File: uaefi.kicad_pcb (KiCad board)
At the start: 4 copper layers, 100 x 136 mm, 150 parts, among them J1 Conn_02x02_Odd_Even, J11 Conn_02x02_Odd_Even, J12 Conn_02x02_Odd_Even, J13 Conn_02x02_Odd_Even, J14 Conn_02x02_Odd_Even, J15 Conn_02x02_Odd_Even, J16 Conn_02x02_Odd_Even, J17 Conn_02x02_Odd_Even, J18 Conn_02x02_Odd_Even, J19 Conn_02x02_Odd_Even, J20 Conn_02x02_Odd_Even, J21 Conn_02x02_Odd_Even, J22 Conn_02x02_Odd_Even, J24 Conn_02x02_Odd_Even, J30 776163-1, J31 776163-1, J6 Conn_01x06, J7 Conn_01x05_Male, J8 USB_B_Mini, J9 USB_C, M1 Module-power_12and5V-0.3, M2 Module-knock-0.2, M3 Module-vr-discrete-0.5, M4 Module-vr-max9924-0.1, M5 Module-wbo-0.5, M6 Module:mega-mcu100/0.3, M7 Module-can-0.1, P1 Pad, P15 Pad, P16 Pad, P17 Pad, P18 Pad, P2 Pad, P3 Pad, P4 Pad, P5 Pad, P6 Pad, P7 Pad, P8 Pad, U1 TLE9201SG, U10 VNLD5160TR-E, U11 VNLD5160TR-E, U2 TLE9201SG, U3 MPX4/MPXH6400_MAP, U4 MAX31855KASA, U5 JDY-33, U6 VNLD5160TR-E, U7 VNLD5160TR-E, U8 VNLD5160TR-E, U9 VNLD5160TR-E

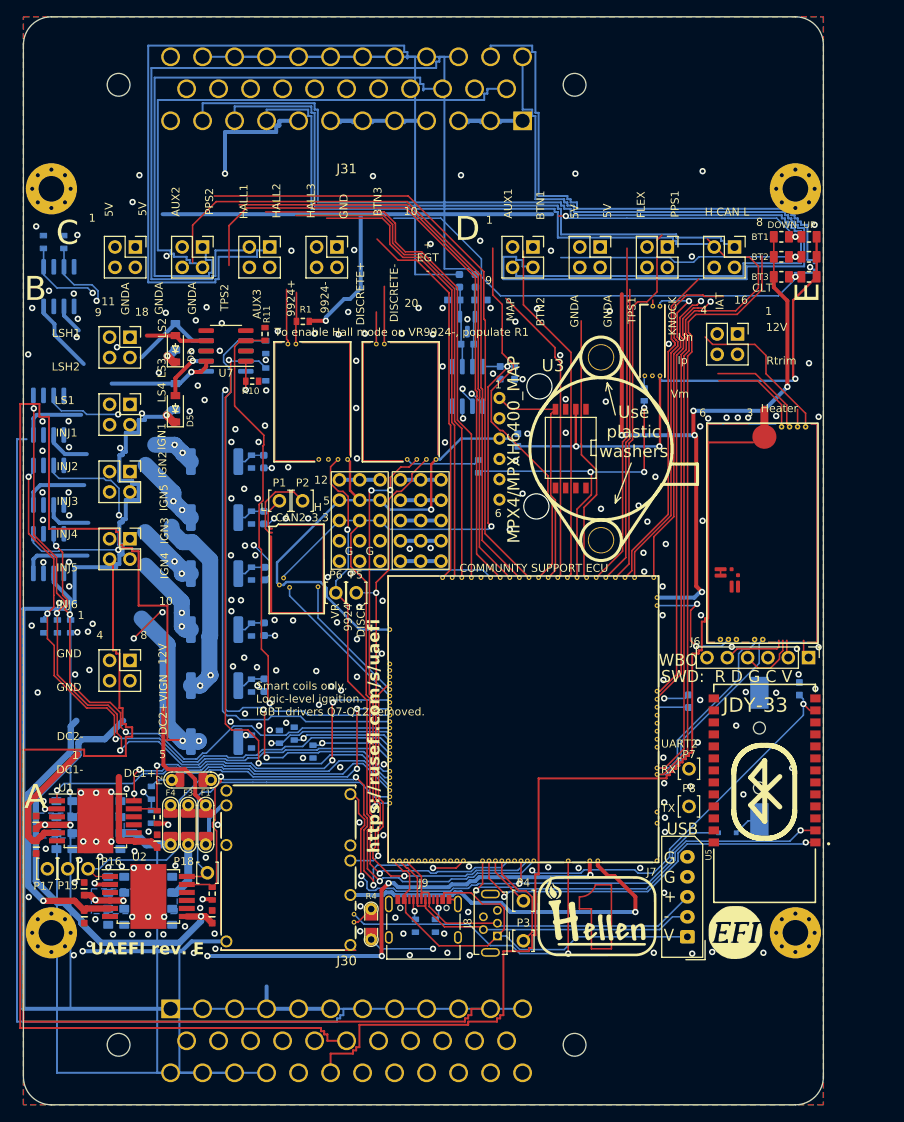
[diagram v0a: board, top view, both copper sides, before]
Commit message: Refill zones, route AMPSEAL pads without shorts, and export KiCad 8 fab files.
Co-authored-by: Quintin <quintinbannink42@users.noreply.github.com>
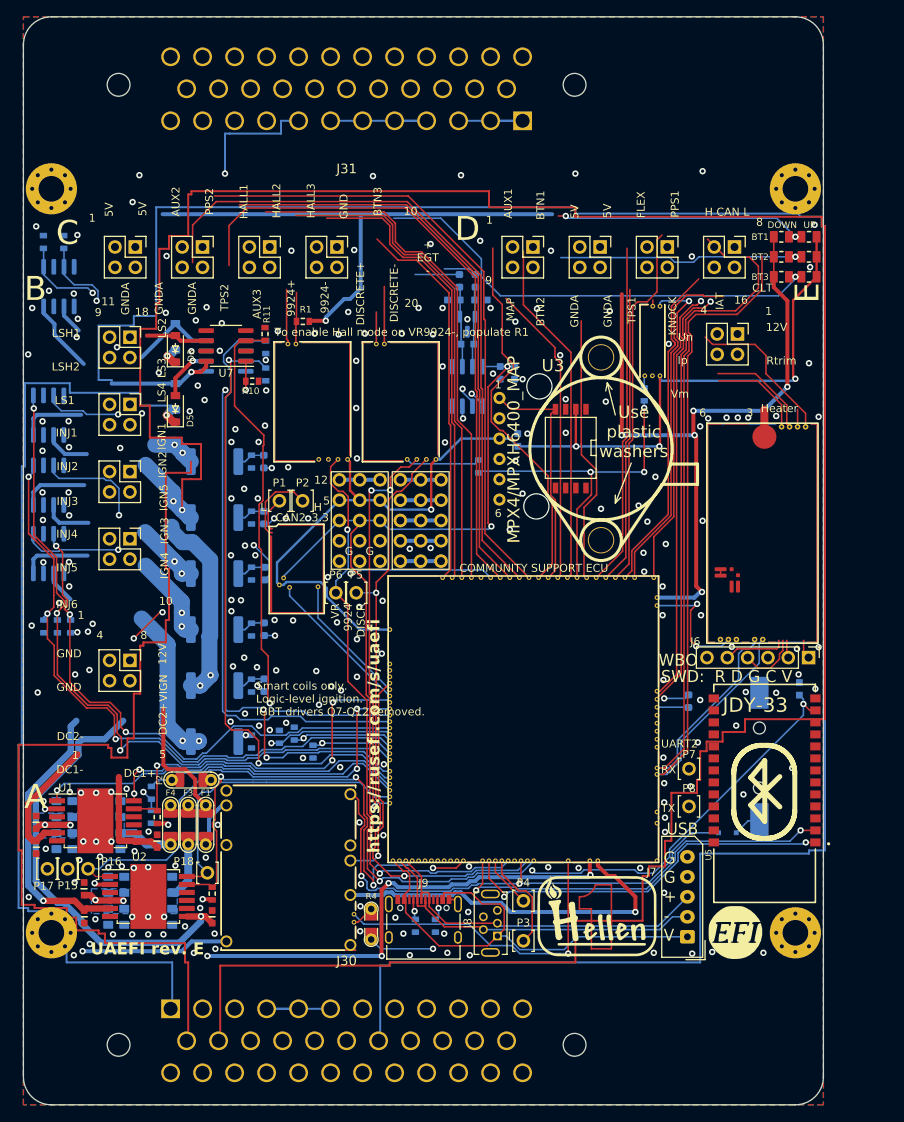
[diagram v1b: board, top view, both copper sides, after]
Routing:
- net /WBO_Rtrim: track 284.2 -> 2.19 mm
- net /OUT_LS4: track 211.3 -> 6.95 mm
- net /VR_DISCRETE+: track 201.0 -> 4.01 mm
- net /OUT_LS_HOT2: track 119.3 -> 314.8 mm
- net /OUT_IGN2: track 133.4 -> 326.4 mm
- net /OUT_LS2: track 190.5 -> 7.69 mm
- net /OUT_IGN6: track 201.9 -> 19.5 mm
- net /VR_MAX9924-: track 179.9 -> 6.49 mm
- net /VR_MAX9924+: track 167.5 -> 6.89 mm
- net /VR_DISCRETE-: track 150.2 -> 7.21 mm
- net /WBO_Ip: track 155.1 -> 13.1 mm
- net /OUT_INJ5: track 143.5 -> 282.9 mm
- net /WBO_Vm: track 150.3 -> 11.9 mm
- net /WBO_Un: track 156.3 -> 19.5 mm
- net /OUT_LS_HOT1: track 140.2 -> 3.77 mm
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
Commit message: Widen the board and route harness nets through a right-edge channel.
Co-authored-by: Quintin <quintinbannink42@users.noreply.github.com>
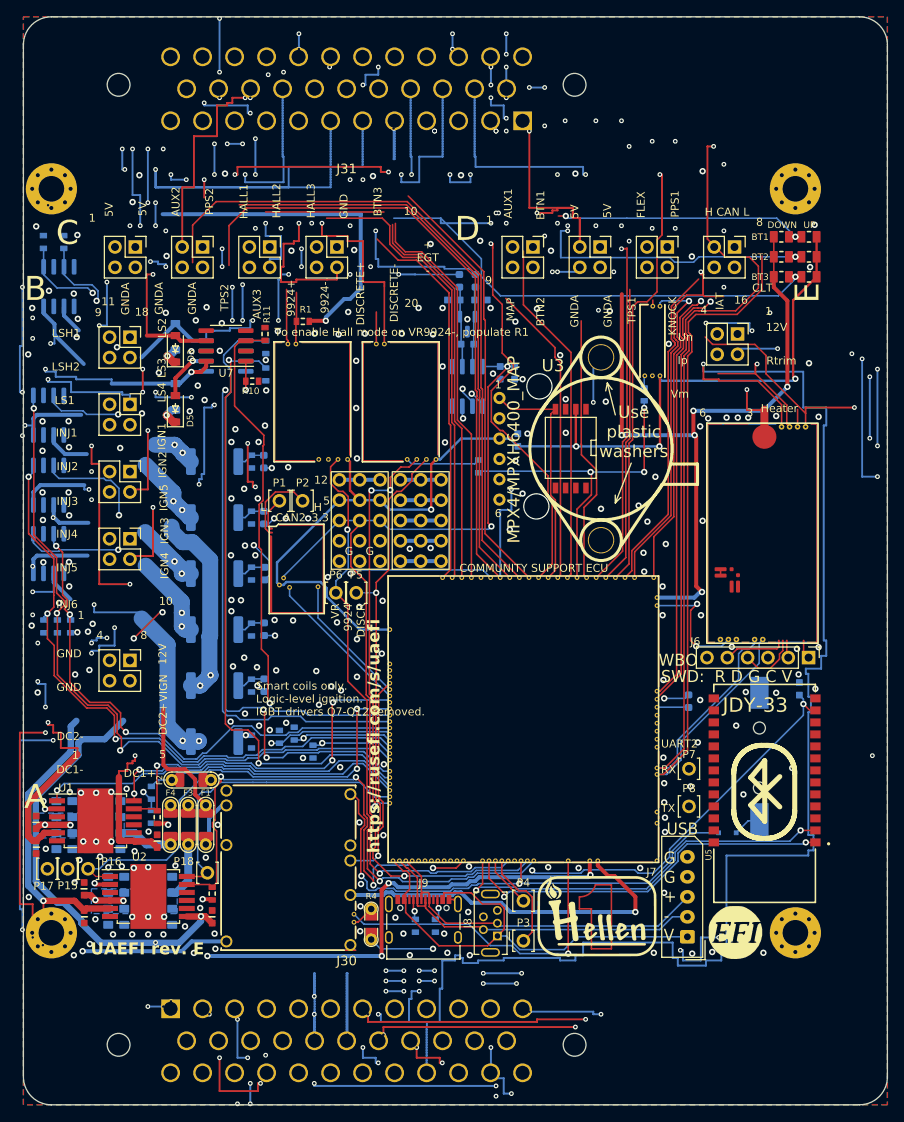
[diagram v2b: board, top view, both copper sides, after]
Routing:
- net /OUT_DC1-: track 17.1 -> 376.1 mm, vias 0 -> 5
- net /OUT_DC1+: track 13.1 -> 355.1 mm, vias 0 -> 5
- net /OUT_INJ6: track 4.09 -> 336.9 mm, vias 0 -> 9
- net /OUT_LS4: track 6.95 -> 338.3 mm, vias 1 -> 6
- net +12V: track 87.3 -> 403.6 mm, vias 0 -> 8
- net /OUT_IGN6: track 19.5 -> 317.7 mm, vias 2 -> 8
- net /OUT_LS2: track 7.69 -> 285.2 mm, vias 0 -> 7
- net /12V_KEY: track 105.2 -> 369.1 mm, vias 0 -> 8
- net /OUT_IGN5: track 24.4 -> 288.2 mm, vias 2 -> 6
- net /OUT_LS_HOT1: track 3.77 -> 264.3 mm, vias 0 -> 4
- net /OUT_LS3: track 10.7 -> 264.0 mm, vias 0 -> 5
- net /OUT_IGN4: track 10.8 -> 256.9 mm, vias 2 -> 3
- net /OUT_INJ1: track 124.4 -> 339.1 mm, vias 0 -> 7
- net /OUT_IGN3: track 8.23 -> 221.8 mm
- net /WBO_Ip: track 13.1 -> 198.5 mm, vias 0 -> 3
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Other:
- board size 100 x 136 mm -> 108 x 136 mm
